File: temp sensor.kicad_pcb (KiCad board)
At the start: 2 copper layers, 48.2 x 24.9 mm, 51 parts, among them IC1 ESP32-C3-MINI-1, J1 USB_C_Receptacle_USB2.0, J2 Conn_01x02_Male, J3 Conn_01x06_Male, J4 USB_B_Micro, J5 Conn_01x02_Male, J6 Conn_01x02_Male, Q1 BC847BDW1, SW1 SW_Push_Right_Angle, SW2 SW_Push_Right_Angle, U1 SHTC3, U2 TLV62569DBV, U3 BME280, U4 Si7020-A20, U5 SN65220

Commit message: Mostly all done, with Rev2. need to do final schematic review and logo
Signed-off-by: lokimetasmith <lokimail@gmail.com>
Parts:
- removed R21, R22: 5.1k, Resistor_SMD:R_0603_1608Metric
- JP1: footprint Jumper:SolderJumper-3_P1.3mm_Bridged12_RoundedPad1.0x1.5mm -> Twig:Jumper_0603_1608Metric
- moved R12 2.88 mm to (149.5, 93.8)
- moved R13 2.34 mm to (149.5, 95.6)
- moved R10 2.15 mm to (152.6, 91.6), turned to 0 degrees
- moved R11 2.14 mm to (152.5, 96.7), turned to 180 degrees
- moved U5 1.05 mm to (152.9, 94.1)
- moved JP1 0.78 mm to (128.0, 95.8)
- moved R20 0.28 mm to (152.7, 98.2)
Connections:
- net /IO20_pico renamed /USB_D-
- net /IO7_pico renamed /USB_D+
- IC1 pad 5: /I37_pico -> (no net)
- IC1 pad 6: /I38_pico -> (no net)
- U5 pad 1: (no net) -> /D+
- U5 pad 3: (no net) -> /D-
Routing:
- net /I38_pico: track 17.3 -> 0.00 mm, vias 2 -> 0
- net GND: track 45.5 -> 59.7 mm, vias 67 -> 72
- net +3V3: track 104.7 -> 112.3 mm
- net /I37_pico: track 4.59 -> 0.00 mm, vias 1 -> 0
- net /V_USB: track 17.1 -> 20.8 mm
- net /USB_D+: track 6.24 -> 2.82 mm
- net /EN: track 32.1 -> 35.4 mm
- net /D+: track 17.3 -> 15.9 mm
- net /IO26_pico: track 21.8 -> 20.6 mm
- net /IO33_pico: track 18.4 -> 17.2 mm
- net /USB_D-: track 1.80 -> 2.85 mm
- net /IO2_pico: track 26.7 -> 27.6 mm
- net /IO13_pico: track 33.1 -> 32.3 mm
- net /IO12_pico: track 5.48 -> 4.79 mm
- net /CC1: track 11.2 -> 11.8 mm, vias 3 -> 2
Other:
- net class USB_Data added: clearance 0.1524, trace_width 0.1524, via_dia 0.6858, via_drill 0.3302
- rule trace_min: 0.2 -> 0.1524
- rule via_min_drill: 0.3 -> 0.254
- rule via_min_size: 0.4 -> 0.508
- board text added: "BOOT"
- board text added: "RST"

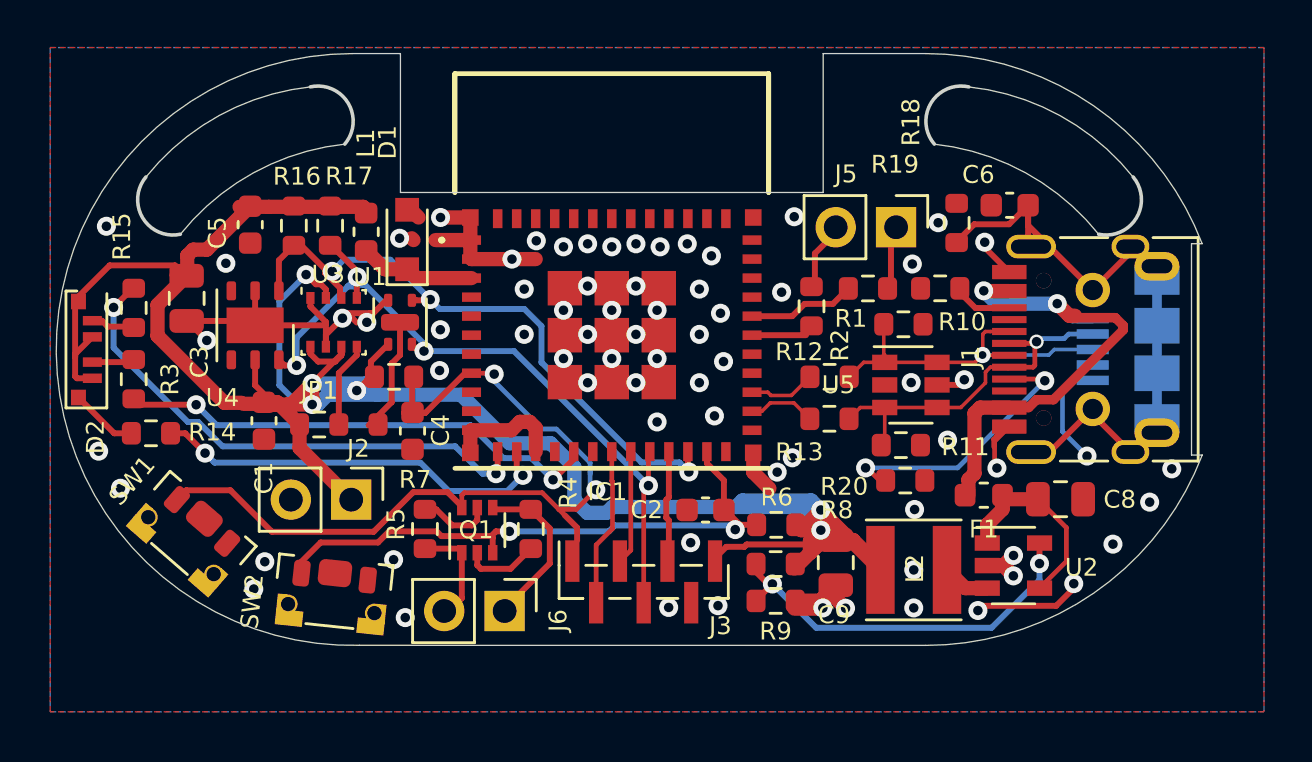
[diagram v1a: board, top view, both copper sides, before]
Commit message: reworked the layout to improve impedance, or so I hope.
Signed-off-by: lokimetasmith <lokimail@gmail.com>
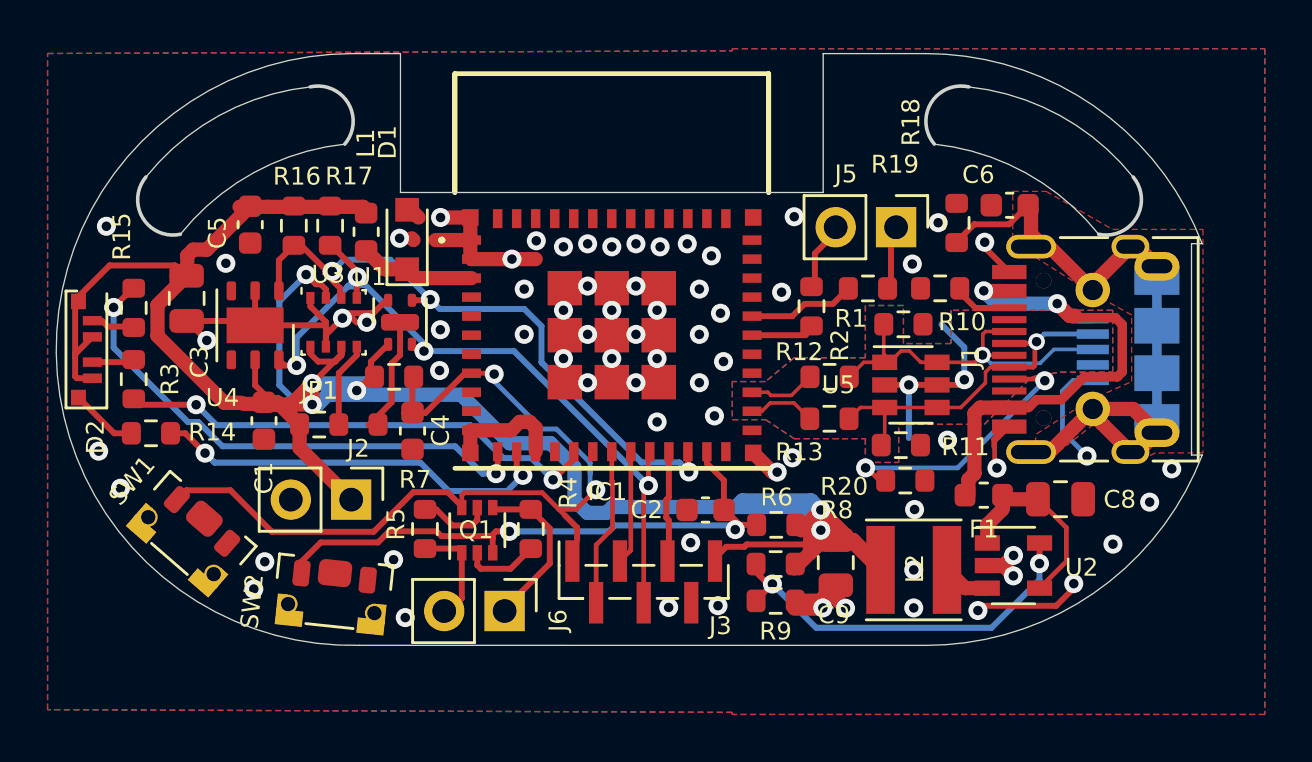
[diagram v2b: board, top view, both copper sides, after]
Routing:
- net GND: track 59.7 -> 66.5 mm
- net /Shield: track 27.8 -> 34.3 mm
- net /V_USB: track 20.8 -> 21.7 mm
- net /D+: track 15.9 -> 16.5 mm
- added copper zone on F.Cu, net /Shield

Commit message: adding graphics and fab notes.
Signed-off-by: lokimetasmith <lokimail@gmail.com>
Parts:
- added REF**: FabDrawing-4Layer, Twig:FabDrawing-2Layer-Metric, F.Cu at (53.4, 21.2)
- added Ref**: Val**, Twig:Juniper_Garden_Vrt_Black, F.Cu at (141.8, 96.8)
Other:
- board text added: "FAB NOTES: UNLESS OTHERWISE SPECIFIED. 1. STANDARDS: A. FABRICATE PCB IN ACCORDANCE WITH THE CURRENT REVISION OF IPC-6012, CLASS 2. B. INTERPRET DIMENSIONS AND TOLERANCES IN ACCORDANCE WITH THE CURRENT REVISION OF ASME Y14.5M. C. DO NOT SCALE DRAWING. 2. MATERIAL: A. FR4 Tg 180 C OR EQUIVALENT. B. EQUIVALENT MATERIAL SHALL BE RoHS COMPLIANT, HALOGEN FREE AND APPROVED BY Juniper Gardens LLC. C. TH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"

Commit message: updated bom, exported gerbers
Signed-off-by: lokimetasmith <lokimail@gmail.com>
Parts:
- removed REF**: FabDrawing-4Layer, Twig:FabDrawing-2Layer-Metric
- removed the Ref** at (141.8, 96.8)
- added REF_stackup: FabDrawing-4Layer, Twig:FabDrawing-2Layer-Metric, F.Cu at (53.6, 19.6)
- added Ref**: Val**, Twig:simplified logo_plain_svg, F.Cu at (144.0, 94.6)
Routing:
- net GND: track 66.5 -> 67.1 mm, vias 72 -> 73
- removed copper zone on F.Cu, net /Shield
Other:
- rule pad_to_mask_clearance: 0.05 -> 0
- board text added: "JuniperTechnology.co"
- board text added: "V0.2"
- board text removed: "FAB NOTES: UNLESS OTHERWISE SPECIFIED. 1. STANDARDS: A. FABRICATE PCB IN ACCORDANCE WITH THE CURRENT REVISION OF IPC-6012, CLASS 2. B. INTERPRET DIMENSIONS AND TOLERANCES IN ACCORDANCE WITH THE CURRENT REVISION OF ASME Y14.5M. C. DO NOT SCALE DRAWING. 2. MATERIAL: A. FR4 Tg 180 C OR EQUIVALENT. B. EQUIVALENT MATERIAL SHALL BE RoHS COMPLIANT, HALOGEN FREE AND APPROVED BY Juniper Gardens LLC. C. TH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"

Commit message: gerbers as ordered for the panelized version 0.2 of the board
Signed-off-by: lokimetasmith <lokimail@gmail.com>
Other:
- outline, holes or cut-outs redrawn
